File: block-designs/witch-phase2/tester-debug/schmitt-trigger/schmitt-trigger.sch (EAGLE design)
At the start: 10 parts, among them IC1 74LVC1G14DBV

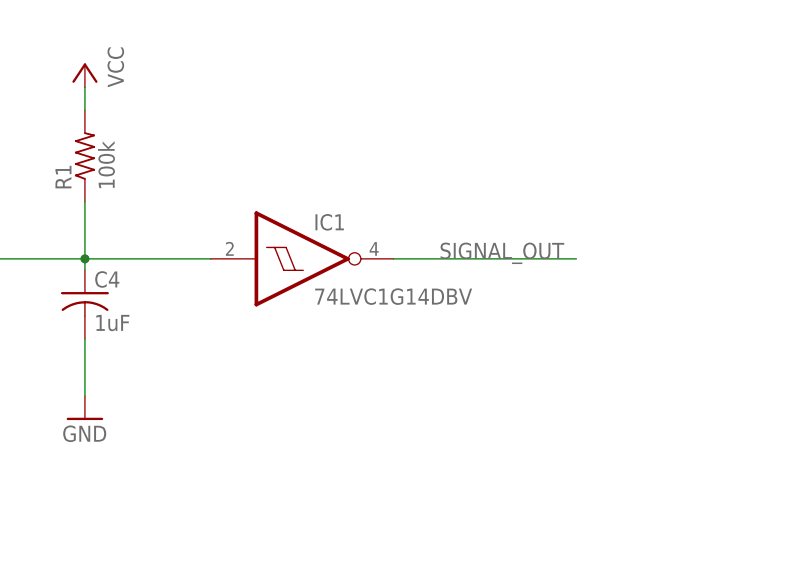
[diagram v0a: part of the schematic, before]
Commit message: change designs to use non-inverting schmitt triggers
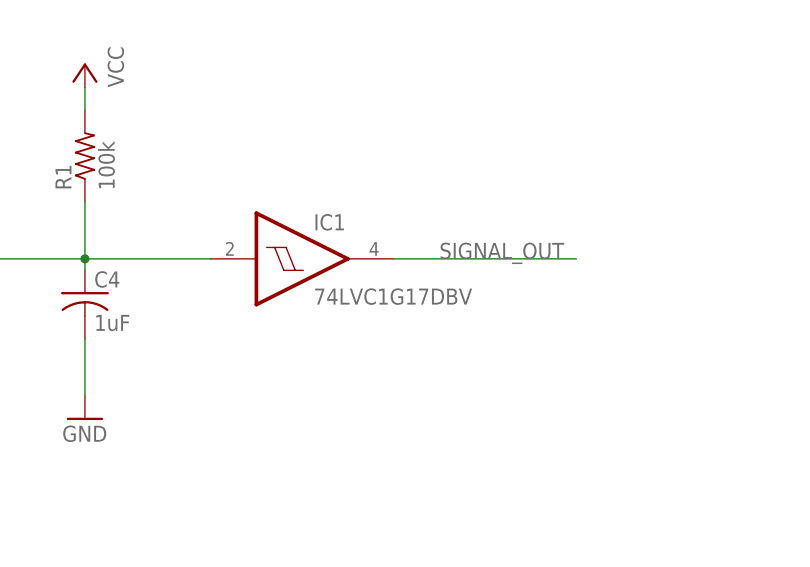
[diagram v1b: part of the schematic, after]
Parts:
- IC1: value 74LVC1G14DBV -> 74LVC1G17DBV; device 74xx-little-us:74LVC1G14DBV -> 74xx-little-us:74LVC1G17DBV
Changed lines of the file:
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@@
 <part name="R1" library="resistor" deviceset="R-US_" device="R0603" value="100k"/>
 <part name="C3" library="resistor" deviceset="C-US" device="C0603K"/>
-<part name="IC1" library="74xx-little-us" deviceset="74*1G14" device="DBV" technology="LVC"/>
+<part name="IC1" library="74xx-little-us" deviceset="74*1G17" device="DBV" technology="LVC"/>
 </parts>
 <sheets>
